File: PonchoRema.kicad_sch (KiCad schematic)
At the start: 0 parts

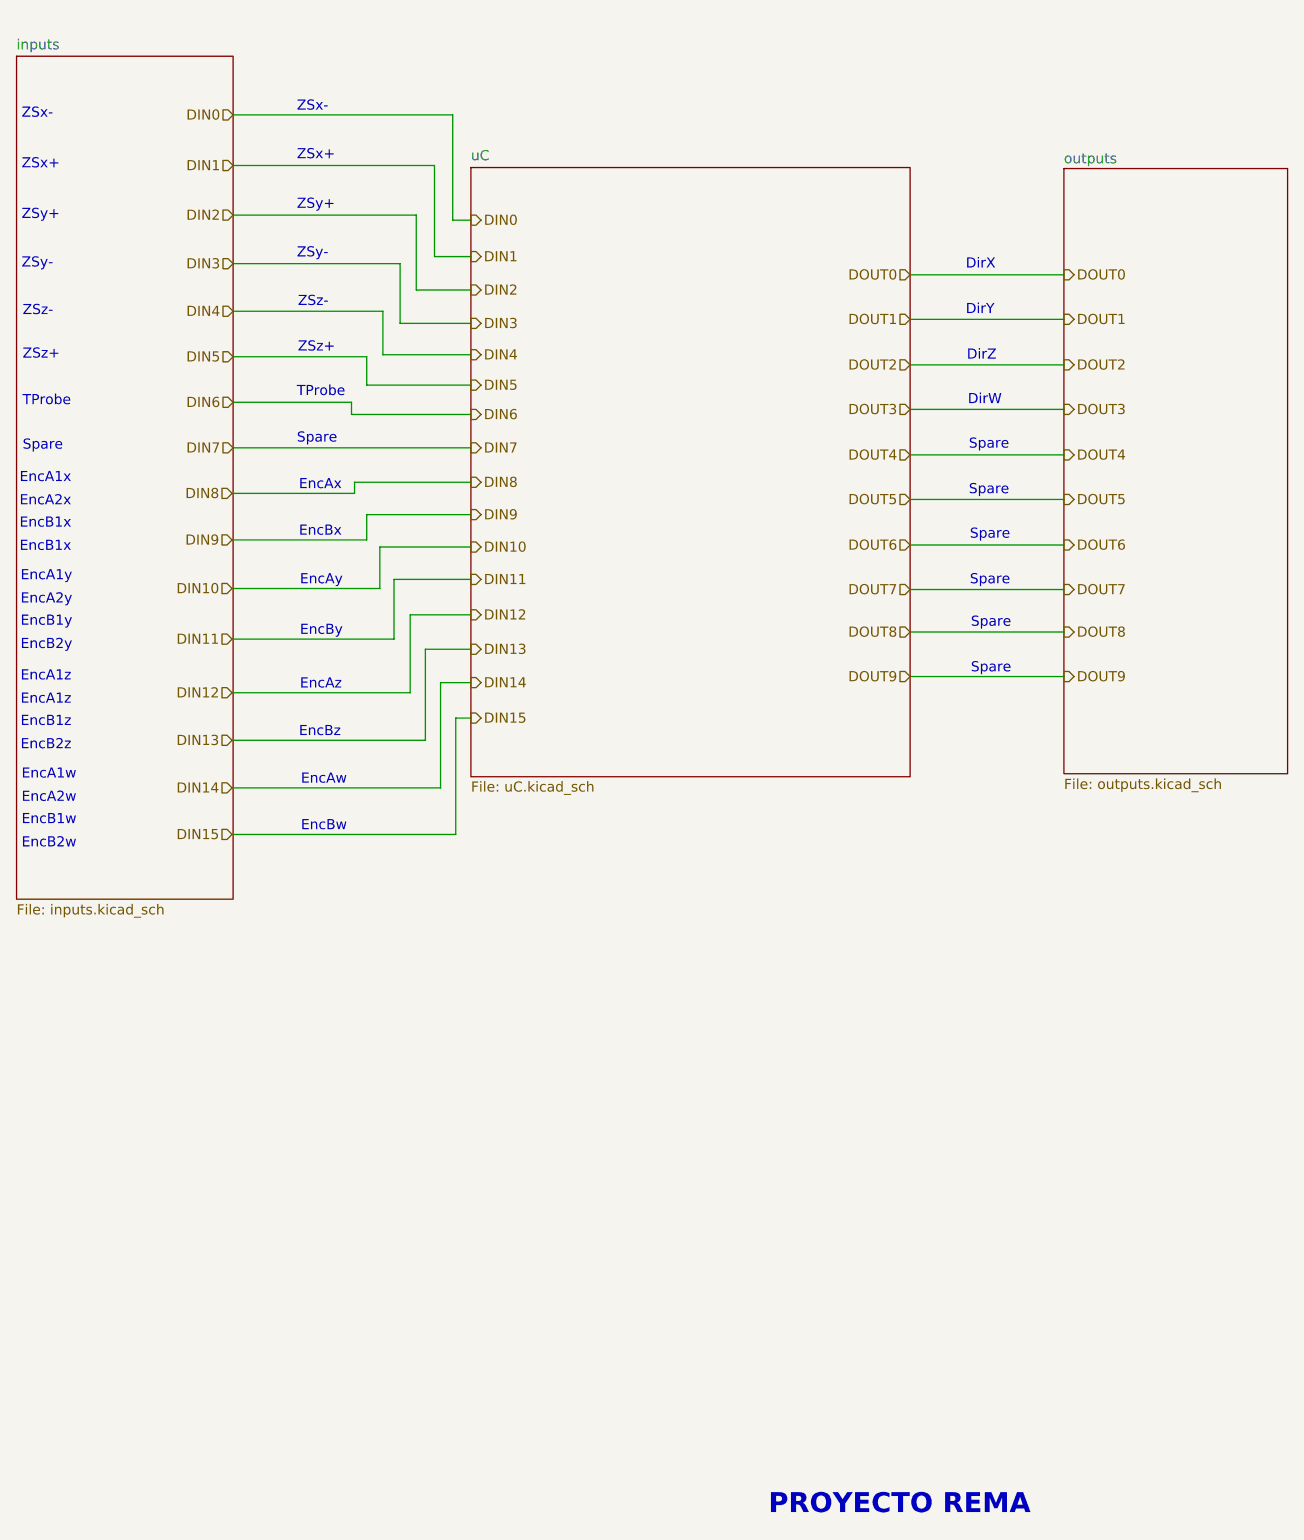
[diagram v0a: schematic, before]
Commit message: Avances en corrección de errores en conexiones eléctricas (ERC).
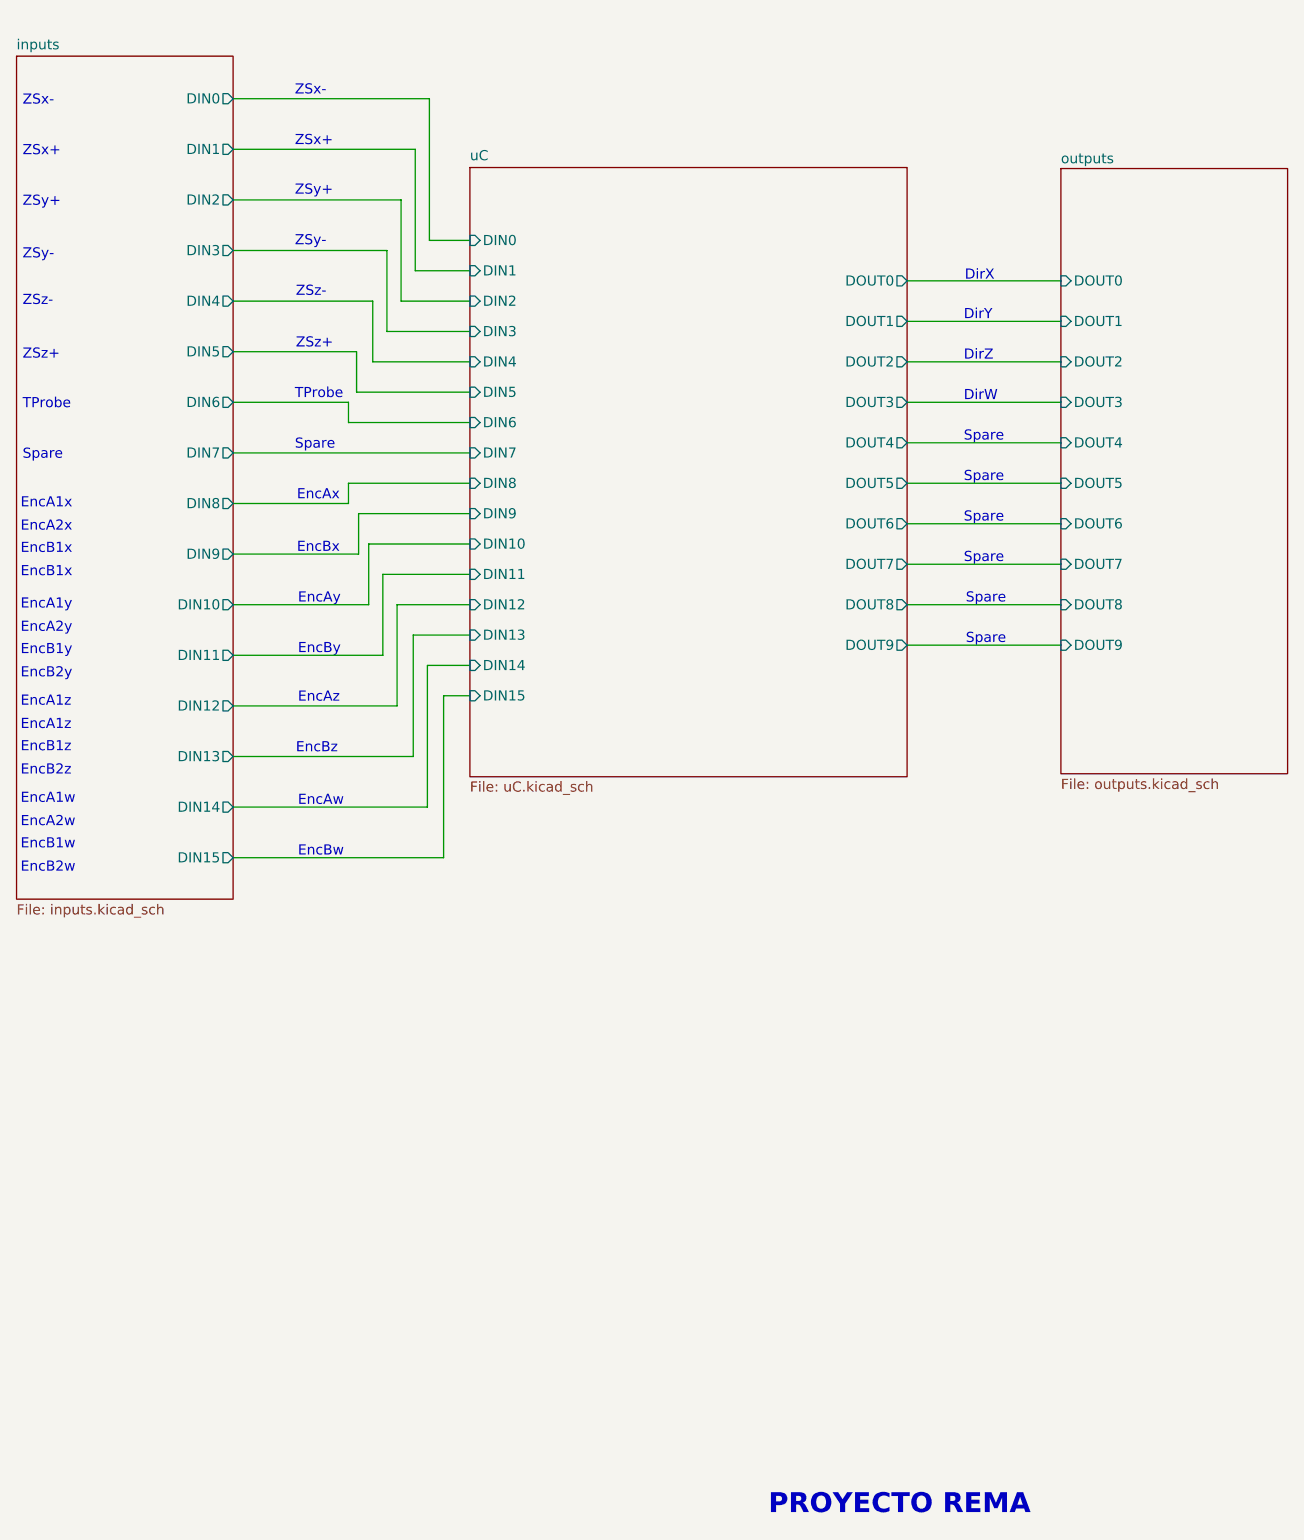
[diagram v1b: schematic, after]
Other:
- sheet inputs ports: added DIN0, DIN1, DIN10, DIN11, DIN12, DIN13, DIN14, DIN15, DIN2, DIN3, DIN4, DIN5, DIN6, DIN7, DIN8, DIN9; removed none
- sheet outputs ports: added DOUT0, DOUT1, DOUT2, DOUT3, DOUT4, DOUT5, DOUT6, DOUT7, DOUT8, DOUT9; removed none
- sheet uC ports: added DIN0, DIN1, DIN10, DIN11, DIN12, DIN13, DIN14, DIN15, DIN2, DIN3, DIN4, DIN5, DIN6, DIN7, DIN8, DIN9, DOUT0, DOUT1, DOUT2, DOUT3, DOUT4, DOUT5, DOUT6, DOUT7, DOUT8, DOUT9; removed none

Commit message: Se corrigieron errores de conexión. Falta asignar footprints aún
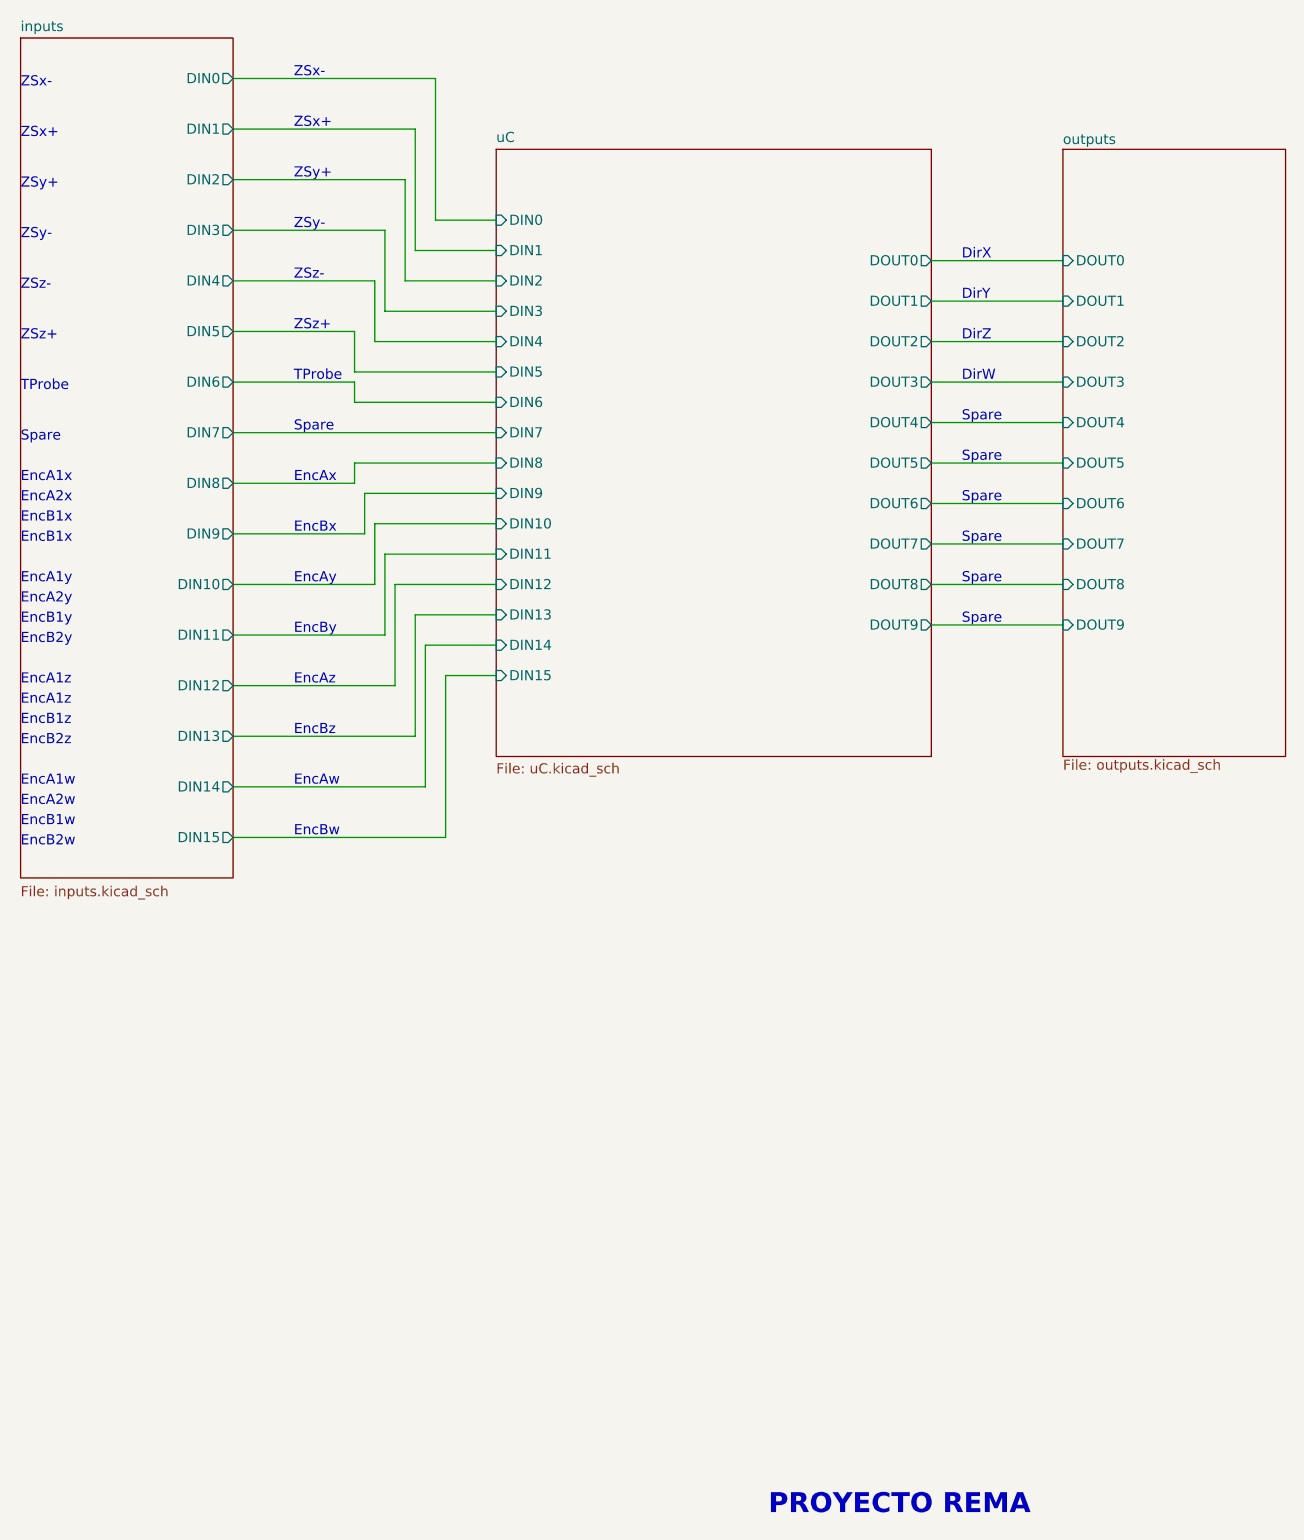
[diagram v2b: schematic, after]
